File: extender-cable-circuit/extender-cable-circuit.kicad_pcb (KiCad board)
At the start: 2 copper layers, 160 x 70 mm, 80 parts, among them X3 24MHz

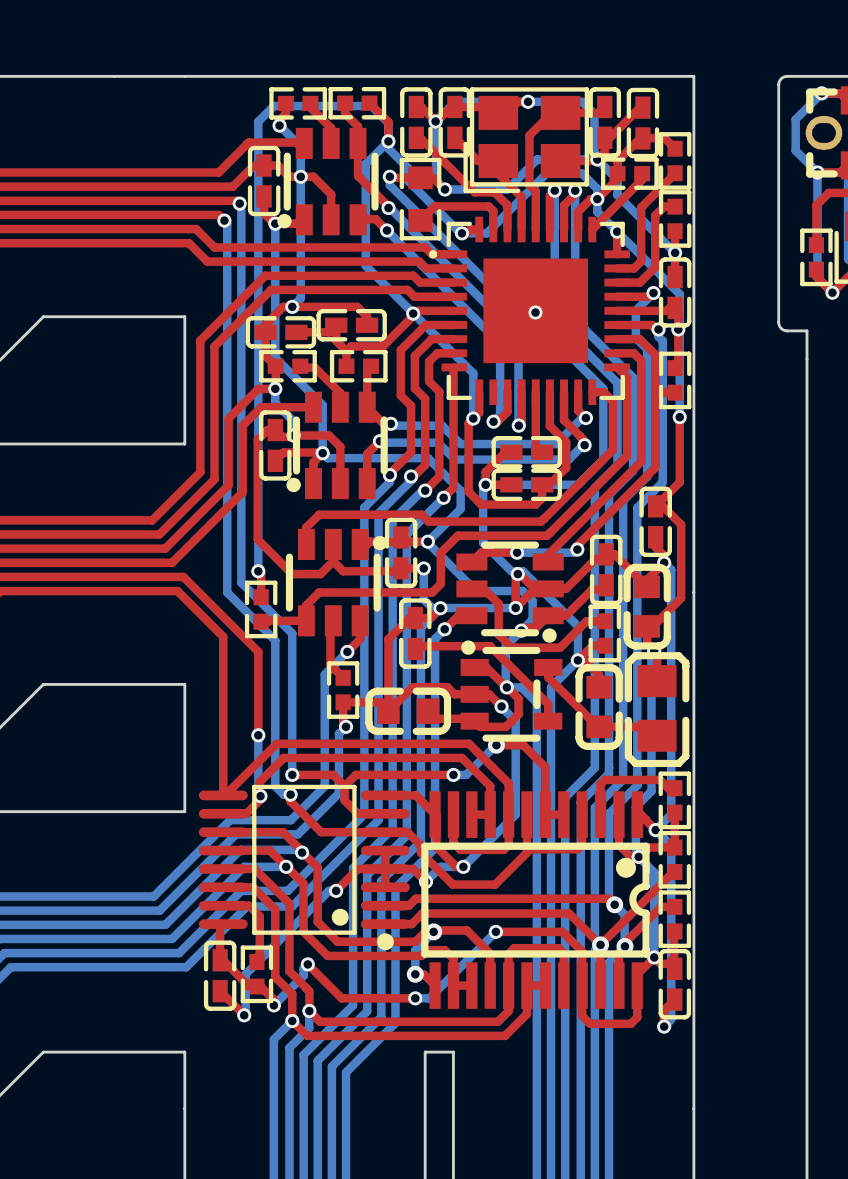
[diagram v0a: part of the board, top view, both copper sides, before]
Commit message: Argh, some chips out of stock, got to do a slight redesign.
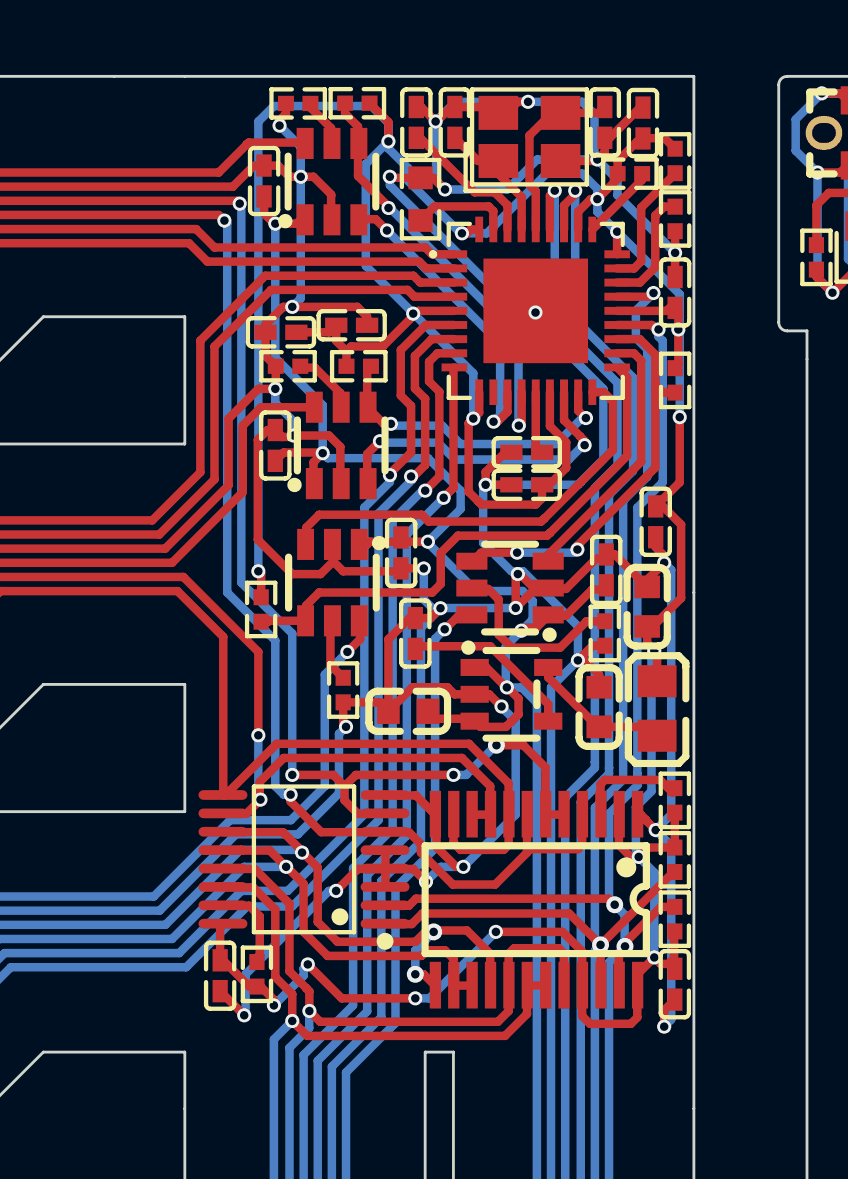
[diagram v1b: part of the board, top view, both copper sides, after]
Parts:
- turned U14 to 180 degrees
- turned U9 to -90 degrees
- turned U23 to 90 degrees
- turned U26 to -90 degrees
- turned U28 to 180 degrees
- turned U7 to 90 degrees
